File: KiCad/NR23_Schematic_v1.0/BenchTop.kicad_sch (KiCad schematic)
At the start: 13 parts, among them M1 Zero_7R_Motor

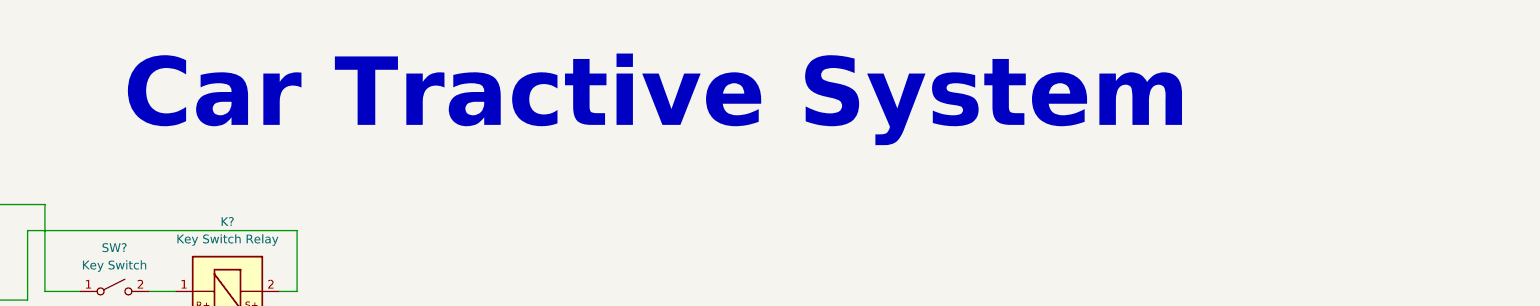
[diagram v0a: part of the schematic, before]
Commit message: added benchtop model schematic
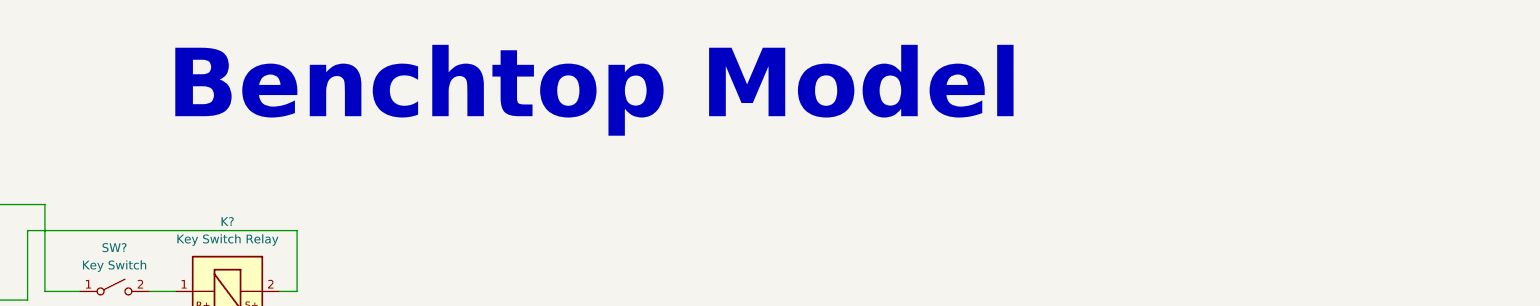
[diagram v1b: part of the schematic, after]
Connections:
- net at U?. (M3): now also J?.2 (Pin_2), J?.4 (Pin_4)
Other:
- note added: "Benchtop Model"
- note removed: "Car Tractive System"
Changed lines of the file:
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@@
     (effects (font (size 1.75 1.75) (thickness 0.254) bold) (justify right bottom))
   )
-  (text "Car Tractive System" (at 73.66 39.37 0)
+  (text "Benchtop Model" (at 80.01 38.1 0)
     (effects (font (size 10 10) (thickness 1) bold) (justify left bottom))
   )

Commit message: Battery update
Made big changes to the battery. Added all 16 battery pins. Started connecting the battery
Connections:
- net at U?. (M3): now also J?.2 (Pin_2), J?.4 (Pin_4)

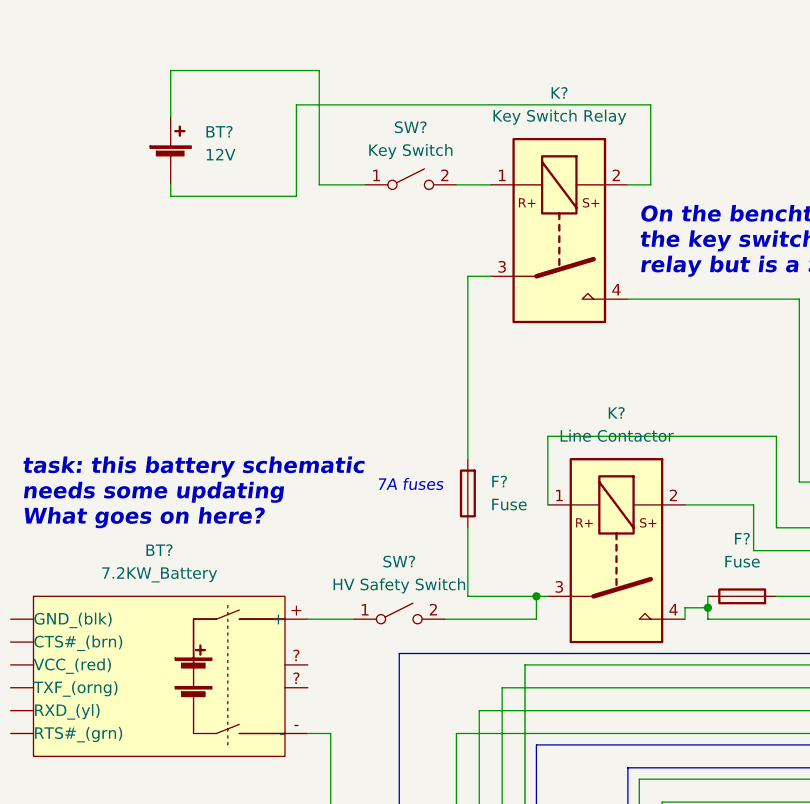
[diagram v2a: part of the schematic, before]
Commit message: added more to the safety circuit
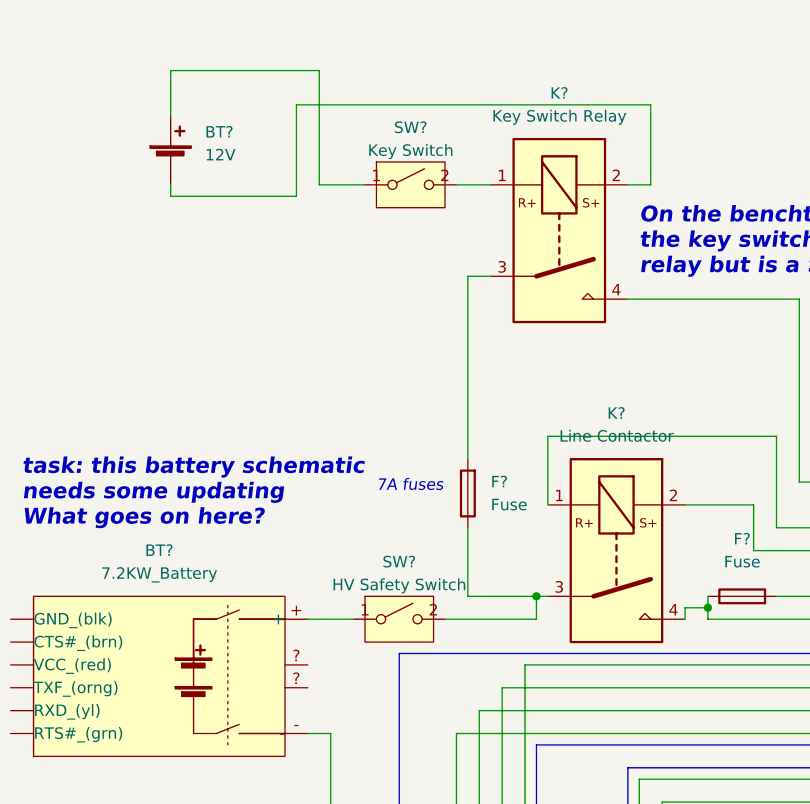
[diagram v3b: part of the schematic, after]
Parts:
- SW? (x2): symbol Switch:SW_SPST -> CamachosSymbols:SW_SPST
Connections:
- net at U?. (M3): now also J?.2 (Pin_2), J?.4 (Pin_4)
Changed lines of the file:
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@@
     (pin "6")
   )
-  (symbol (lib_id "Switch:SW_SPST") (at 72.39 62.23 0) (unit 1)
+  (symbol (lib_id "CamachosSymbols:SW_SPST") (at 72.39 62.23 0) (unit 1)
     (in_bom yes) (on_board yes) (fields_autoplaced)
     (property "Reference" "SW?" (id 0) (at 72.39 55.88 0))
@@
     (pin "2")
   )
-  (symbol (lib_id "Switch:SW_SPST") (at 71.12 110.49 0) (unit 1)
+  (symbol (lib_id "CamachosSymbols:SW_SPST") (at 71.12 110.49 0) (unit 1)
     (in_bom yes) (on_board yes) (fields_autoplaced)
     (property "Reference" "SW?" (id 0) (at 71.12 104.14 0))

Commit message: Added Dash to Schematic
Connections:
- net at U?. (M3): now also J?.2 (Pin_2), J?.4 (Pin_4)

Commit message: worked some more on emergency stop switches
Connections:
- net at U?. (M3): now also J?.2 (Pin_2), J?.4 (Pin_4)

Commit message: added TI board box on the Tractive System Schematc
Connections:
- net at U?. (M3): now also J?.2 (Pin_2), J?.4 (Pin_4)

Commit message: endish of day 05APR23
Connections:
- net at U?. (M3): now also J?.2 (Pin_2), J?.4 (Pin_4)

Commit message: end of day 05APR23
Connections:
- net at U?. (M3): now also J?.2 (Pin_2), J?.4 (Pin_4)
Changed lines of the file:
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@@
 (kicad_sch (version 20211123) (generator eeschema)
-  (paper "A")
+  (paper "User" 334.01 216.002)
   (title_block
     (title "Tractive System")
